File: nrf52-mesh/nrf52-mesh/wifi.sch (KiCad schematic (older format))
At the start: 1 part

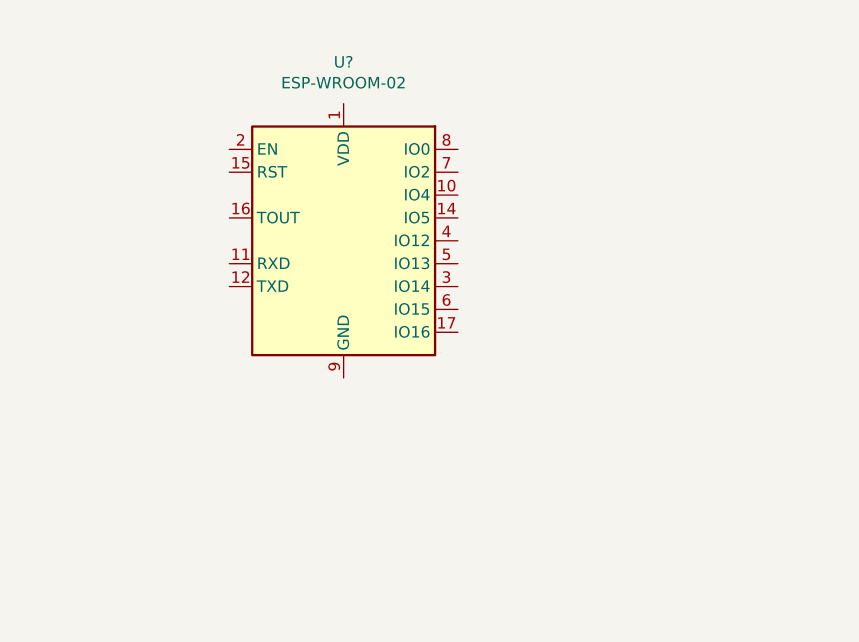
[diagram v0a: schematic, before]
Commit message: nRF52 + ESP WROOM
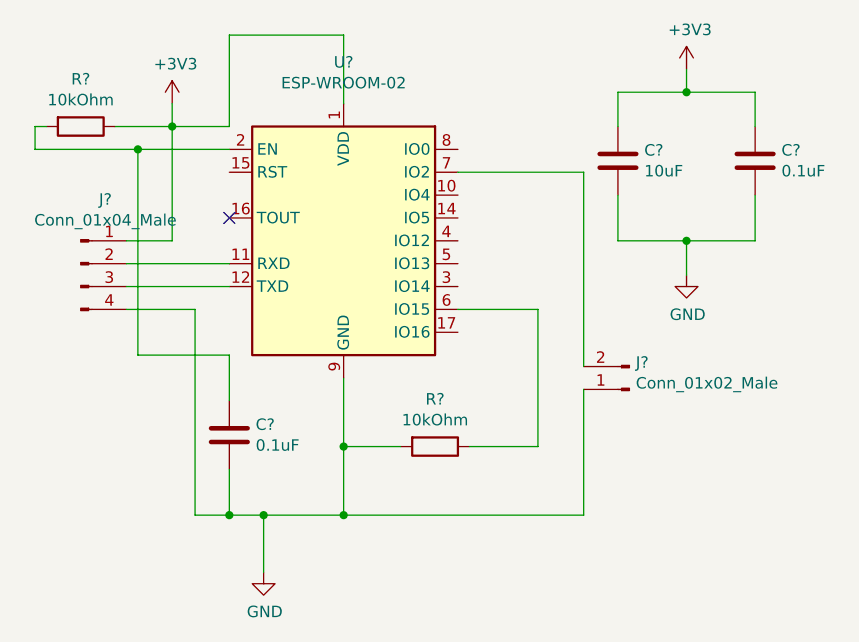
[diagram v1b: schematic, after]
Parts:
- added C?: 0.1uF, Resistor_SMD:R_0402_1005Metric, symbol Device:C
- added C?: 10uF, Capacitor_SMD:C_0402_1005Metric, symbol Device:C
- added C?: 0.1uF, Capacitor_SMD:C_0402_1005Metric, symbol Device:C
- added J?: Conn_01x04_Male, symbol Connector:Conn_01x04_Male
- added J?: Conn_01x02_Male, symbol Connector:Conn_01x02_Male
- added R? (x2): 10kOhm, Resistor_SMD:R_0402_1005Metric, symbol Device:R
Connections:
- net +3V3: now reaches U?.1 (VDD)
- net +3V3: now also C?.1, C?.1, J?.1 (Pin_1), R?.1
- net at U?.11 (RXD): now also J?.2 (Pin_2)
- net at U?.12 (TXD): now also J?.3 (Pin_3)
- net GND: now reaches U?.13 (GND), U?.18 (GND), U?.19 (GND), U?.9 (GND)
- net GND: now also C?.2, C?.2, C?.2, J?.1 (Pin_1), J?.4 (Pin_4), R?.2
- net at U?.2 (EN): now also C?.1, R?.2
- net at U?.6 (IO15): now also R?.1
- net at U?.7 (IO2): now also J?.2 (Pin_2)
- no-connect marks 0 -> 1
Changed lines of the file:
@@
 	1    0    0    -1
 $EndComp
+$Comp
+L Connector:Conn_01x04_Male J?
+U 1 1 5E8D293C
+P 3950 3000
+F 0 "J?" H 4058 3281 50  0000 C CNN
+F 1 "Conn_01x04_Male" H 4058 3190 50  0000 C CNN
+F 2 "" H 3950 3000 50  0001 C CNN
+F 3 "~" H 3950 3000 50  0001 C CNN
+	1    3950 3000
+	1    0    0    -1
+$EndComp
+Wire Wire Line
+	4150 3000 4600 3000
+Wire Wire Line
+	4150 3100 4600 3100
+Wire Wire Line
+	4150 3200 4450 3200
+Wire Wire Line
+	4450 3200 4450 4100
+Wire Wire Line
+	4450 4100 4600 4100
+Wire Wire Line
+	5100 4100 5100 3800
+$Comp
+L power:GND #PWR?
+U 1 1 5E8D39E4
+P 4750 4350
+F 0 "#PWR?" H 4750 4100 50  0001 C CNN
+F 1 "GND" H 4755 4177 50  0000 C CNN
+F 2 "" H 4750 4350 50  0001 C CNN
+F 3 "" H 4750 4350 50  0001 C CNN
+	1    4750 4350
+	1    0    0    -1
+$EndComp
+Wire Wire Line
+	4750 4350 4750 4100
+Connection ~ 4750 4100
+Wire Wire Line
+	4750 4100 5100 4100
+$Comp
+L power:+3V3 #PWR?
+U 1 1 5E8D4396
+P 4350 2300
+F 0 "#PWR?" H 4350 2150 50  0001 C CNN
+F 1 "+3V3" H 4365 2473 50  0000 C CNN
+F 2 "" H 4350 2300 50  0001 C CNN
+F 3 "" H 4350 2300 50  0001 C CNN
+	1    4350 2300
+	1    0    0    -1
+$EndComp
+Wire Wire Line
+	4150 2900 4350 2900
+Wire Wire Line
+	4350 2900 4350 2400
+$Comp
+L Device:R R?
+U 1 1 5E8D4A39
+P 3950 2400
+F 0 "R?" V 3743 2400 50  0000 C CNN
+F 1 "10kOhm" V 3834 2400 50  0000 C CNN
+F 2 "Resistor_SMD:R_0402_1005Metric" V 3880 2400 50  0001 C CNN
+F 3 "~" H 3950 2400 50  0001 C CNN
+	1    3950 2400
+	0    1    1    0
+$EndComp
+Wire Wire Line
+	4350 2400 4100 2400
+Connection ~ 4350 2400
+Wire Wire Line
+	4350 2400 4350 2300
+Wire Wire Line
+	3800 2400 3750 2400
+Wire Wire Line
+	3750 2400 3750 2500
+Wire Wire Line
+	3750 2500 4200 2500
+$Comp
+L Device:C C?
+U 1 1 5E8D57B1
+P 4600 3750
+F 0 "C?" H 4715 3796 50  0000 L CNN
+F 1 "0.1uF" H 4715 3705 50  0000 L CNN
+F 2 "Resistor_SMD:R_0402_1005Metric" H 4638 3600 50  0001 C CNN
+F 3 "~" H 4600 3750 50  0001 C CNN
+	1    4600 3750
+	1    0    0    -1
+$EndComp
+Wire Wire Line
+	4600 3900 4600 4100
+Connection ~ 4600 4100
+Wire Wire Line
+	4600 4100 4750 4100
+Wire Wire Line
+	4600 3600 4600 3400
+Wire Wire Line
+	4600 3400 4200 3400
+Wire Wire Line
+	4200 3400 4200 2500
+Connection ~ 4200 2500
+Wire Wire Line
+	4200 2500 4600 2500
+Wire Wire Line
+	4600 2400 4600 2000
+Wire Wire Line
+	4600 2000 5100 2000
+Wire Wire Line
+	5100 2000 5100 2300
+Wire Wire Line
+	4350 2400 4600 2400
+$Comp
+L Device:C C?
+U 1 1 5E8D9846
+P 6300 2550
+AR Path="/5E8D9846" Ref="C?"  Part="1"
+AR Path="/5E4CCB9A/5E8D9846" Ref="C?"  Part="1"
+AR Path="/5E4EF39F/5E8D9846" Ref="C?"  Part="1"
+AR Path="/5E8D2EF3/5E8D9846" Ref="C?"  Part="1"
+F 0 "C?" H 6415 2596 50  0000 L CNN
+F 1 "10uF" H 6415 2505 50  0000 L CNN
+F 2 "Capacitor_SMD:C_0402_1005Metric" H 6338 2400 50  0001 C CNN
+F 3 "~" H 6300 2550 50  0001 C CNN
+	1    6300 2550
+	1    0    0    -1
+$EndComp
+$Comp
+L Device:C C?
+U 1 1 5E8D984C
+P 6900 2550
+AR Path="/5E8D984C" Ref="C?"  Part="1"
+AR Path="/5E4CCB9A/5E8D984C" Ref="C?"  Part="1"
+AR Path="/5E4EF39F/5E8D984C" Ref="C?"  Part="1"
+F 0 "C?" H 7015 2596 50  0000 L CNN
+F 1 "0.1uF" H 7015 2505 50  0000 L CNN
+F 2 "Capacitor_SMD:C_0402_1005Metric" H 6938 2400 50  0001 C CNN
+F 3 "~" H 6900 2550 50  0001 C CNN
+	1    6900 2550
+	1    0    0    -1
+$EndComp
+$Comp
+L power:GND #PWR?
+U 1 1 5E8D9852
+P 6600 3050
+AR Path="/5E8D9852" Ref="#PWR?"  Part="1"
+AR Path="/5E4CCB9A/5E8D9852" Ref="#PWR?"  Part="1"
+AR Path="/5E4EF39F/5E8D9852" Ref="#PWR?"  Part="1"
+F 0 "#PWR?" H 6600 2800 50  0001 C CNN
+F 1 "GND" H 6605 2877 50  0000 C CNN
+F 2 "" H 6600 3050 50  0001 C CNN
+F 3 "" H 6600 3050 50  0001 C CNN
+	1    6600 3050
+	1    0    0    -1
+$EndComp
+$Comp
+L power:+3V3 #PWR?
+U 1 1 5E8D9858
+P 6600 2150
+AR Path="/5E8D9858" Ref="#PWR?"  Part="1"
+AR Path="/5E4CCB9A/5E8D9858" Ref="#PWR?"  Part="1"
+AR Path="/5E4EF39F/5E8D9858" Ref="#PWR?"  Part="1"
+F 0 "#PWR?" H 6600 2000 50  0001 C CNN
+F 1 "+3V3" H 6615 2323 50  0000 C CNN
+F 2 "" H 6600 2150 50  0001 C CNN
+F 3 "" H 6600 2150 50  0001 C CNN
+	1    6600 2150
+	1    0    0    -1
+$EndComp
+Wire Wire Line
+	6300 2400 6300 2250
+Wire Wire Line
+	6300 2250 6600 2250
+Wire Wire Line
+	6600 2250 6600 2150
+Wire Wire Line
+	6600 2250 6900 2250
+Wire Wire Line
+	6900 2250 6900 2400
+Connection ~ 6600 2250
+Wire Wire Line
+	6300 2700 6300 2900
+Wire Wire Line
+	6300 2900 6600 2900
+Wire Wire Line
+	6600 2900 6600 3050
+Wire Wire Line
+	6600 2900 6900 2900
+Wire Wire Line
+	6900 2900 6900 2700
+Connection ~ 6600 2900
+$Comp
+L Device:R R?
+U 1 1 5E8DABDD
+P 5500 3800
+F 0 "R?" V 5293 3800 50  0000 C CNN
+F 1 "10kOhm" V 5384 3800 50  0000 C CNN
+F 2 "Resistor_SMD:R_0402_1005Metric" V 5430 3800 50  0001 C CNN
+F 3 "~" H 5500 3800 50  0001 C CNN
+	1    5500 3800
+	0    1    1    0
+$EndComp
+Wire Wire Line
+	5600 3200 5950 3200
+Wire Wire Line
+	5950 3200 5950 3800
+Wire Wire Line
+	5950 3800 5650 3800
+Wire Wire Line
+	5100 3800 5350 3800
+Connection ~ 5100 3800
+Wire Wire Line
+	5100 3800 5100 3500
+$Comp
+L Connector:Conn_01x02_Male J?
+U 1 1 5E8DDB3A
+P 6350 3550
+F 0 "J?" H 6322 3432 50  0000 R CNN
+F 1 "Conn_01x02_Male" H 6322 3523 50  0000 R CNN
+F 2 "" H 6350 3550 50  0001 C CNN
+F 3 "~" H 6350 3550 50  0001 C CNN
+	1    6350 3550
+	-1   0    0    1
+$EndComp
+Wire Wire Line
+	5600 2600 6150 2600
+Wire Wire Line
+	6150 2600 6150 3450
+Wire Wire Line
+	6150 4100 5100 4100
+Connection ~ 5100 4100
+Wire Wire Line
+	6150 3550 6150 4100
+NoConn ~ 4600 2800
 $EndSCHEMATC
